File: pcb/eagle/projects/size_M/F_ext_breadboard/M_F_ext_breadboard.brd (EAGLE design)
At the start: 10 parts

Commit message: PCB M.1
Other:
- board text added: "breadboard M.1"
- board text removed: "breadbrd M.1"

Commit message: PCB M.3
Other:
- board text added: "breadboard M.3"
- board text removed: "breadboard M.1"

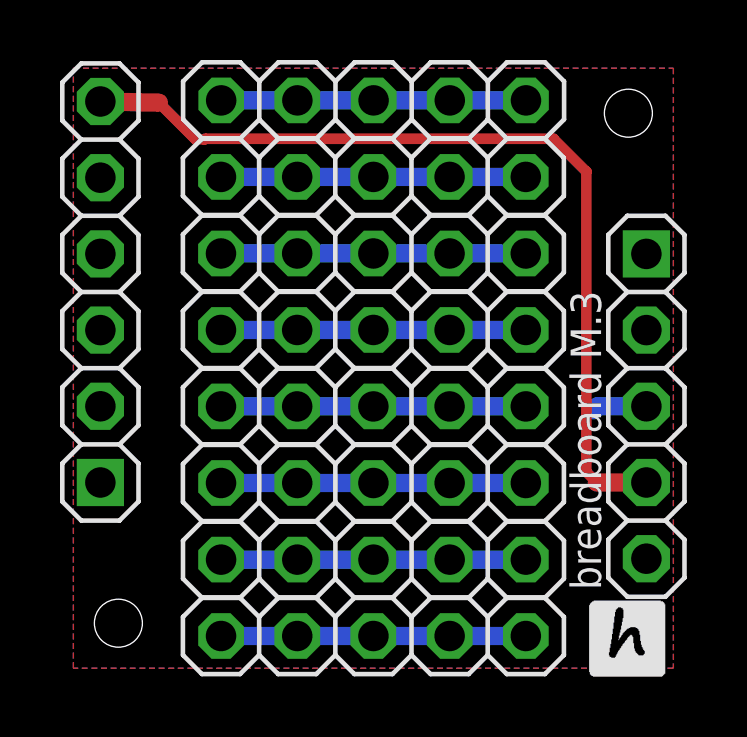
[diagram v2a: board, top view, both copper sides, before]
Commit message: reorganized pcb folders
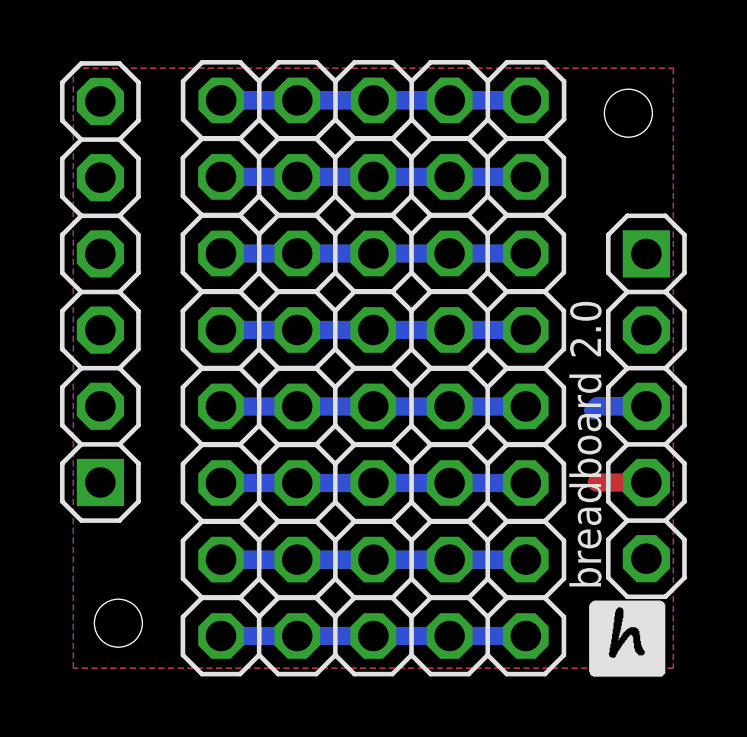
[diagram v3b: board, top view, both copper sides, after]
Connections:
- net GND: no longer JP2.6
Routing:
- net GND: track 29.3 -> 1.65 mm
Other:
- board text added: "breadboard 2.0"
- board text removed: "breadboard M.3"
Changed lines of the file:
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@@
 <hole x="2" y="2" drill="1.6"/>
 <circle x="2" y="2" radius="1.9" width="0.1" layer="52"/>
-<text x="18.0898" y="3.1106" size="1.016" layer="21" rot="R90">breadboard M.3</text>
+<text x="18.0898" y="3.1106" size="1.016" layer="21" rot="R90">breadboard 2.0</text>
 <rectangle x1="17.8181" y1="0.2159" x2="20.1295" y2="0.2413" layer="21"/>
 <rectangle x1="17.7673" y1="0.2413" x2="20.1549" y2="0.2667" layer="21"/>
@@
 <vertex x="0.5" y="0.5"/>
 </polygon>
-<contactref element="JP2" pad="6"/>
-<wire x1="1.4" y1="19.39" x2="3.35" y2="19.35" width="0.6096" layer="1"/>
-<wire x1="17.5998" y1="17.05345625" x2="17.5998" y2="7.0382" width="0.3556" layer="1"/>
-<wire x1="3.35" y1="19.35" x2="4.5716" y2="18.1284" width="0.3556" layer="1"/>
-<wire x1="4.5716" y1="18.1284" x2="4.87614375" y2="18.1284" width="0.3556" layer="1"/>
-<wire x1="4.87614375" y1="18.1284" x2="4.89394375" y2="18.1462" width="0.3556" layer="1"/>
-<wire x1="4.89394375" y1="18.1462" x2="16.50705625" y2="18.1462" width="0.3556" layer="1"/>
-<wire x1="16.50705625" y1="18.1462" x2="17.5998" y2="17.05345625" width="0.3556" layer="1"/>
 <contactref element="JP11" pad="4"/>
 <wire x1="19.6" y1="6.69" x2="17.948" y2="6.69" width="0.6096" layer="1"/>
-<wire x1="17.948" y1="6.69" x2="17.5998" y2="7.0382" width="0.3556" layer="1"/>
 </signal>
 <signal name="VDD">

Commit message: PCB v7 * 14 pin attiny is main adapter chip now. * changed adapter pin meaning (a1-a5, swapped RX-TX, VUSB replaced by A5, top most pin changed from GND to A4) * changed usb chip of main board
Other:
- board text added: "breadboard M7"
- board text removed: "breadboard 2.0"
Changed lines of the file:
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@@
 <hole x="2" y="2" drill="1.6"/>
 <circle x="2" y="2" radius="1.9" width="0.1" layer="52"/>
-<text x="18.0898" y="3.1106" size="1.016" layer="21" rot="R90">breadboard 2.0</text>
+<text x="18.0898" y="3.1106" size="1.016" layer="21" rot="R90">breadboard M7</text>
 <rectangle x1="17.8181" y1="0.2159" x2="20.1295" y2="0.2413" layer="21"/>
 <rectangle x1="17.7673" y1="0.2413" x2="20.1549" y2="0.2667" layer="21"/>
@@
 <signals>
 <signal name="GND">
-<polygon width="0.3048" layer="1" isolate="0.3048">
+<polygon width="0.254" layer="1" isolate="0.254">
 <vertex x="0.5" y="20.5"/>
 <vertex x="20.5" y="20.5"/>
@@
 </signal>
 <signal name="VDD">
-<polygon width="0.3048" layer="16" isolate="0.3048">
+<polygon width="0.254" layer="16" isolate="0.254">
 <vertex x="0.5" y="20.5"/>
 <vertex x="20.5" y="20.5"/>
